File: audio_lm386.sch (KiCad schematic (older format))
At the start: 14 parts, among them J1 Screw_Terminal_01x02, J2 Screw_Terminal_01x02, J3 ST-025, U1 LM386

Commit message: добавлен предусилитель с пинами для подключения потенциометра
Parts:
- added C2: 47n, Capacitor_SMD:C_0805_2012Metric, symbol Device:C
- added C3, C4: 10uF, Capacitor_SMD:C_1206_3216Metric, symbol Device:CP
- added C5: 2n2, Capacitor_SMD:C_0805_2012Metric, symbol Device:C
- added J2: Screw_Terminal_01x03, Connector_PinHeader_2.54mm:PinHeader_1x03_P2.54mm_Vertical, symbol Connector:Screw_Terminal_01x03
- added Q1: MMBT5551L, Package_TO_SOT_SMD:SOT-23, symbol Transistor_BJT:MMBT5551L
- added R2, R3, R4, R5, R6: 10k, Resistor_SMD:R_0805_2012Metric, symbol Device:R
- J4: renamed from J3; footprint Connector_Audio:Jack_3.5mm_CUI_SJ1-3533NG_Horizontal_CircularHoles -> AM_Radio:ST-025 audio_jack
- renumbered C6 to C10, C3 to C6, C2 to C7, C4 to C8, C5 to C9, J2 to J3, R3 to R7, R2 to R8
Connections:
- net GND: now also C3.2, C5.2, J2.3 (Pin_3), R5.1
- net at C1.1, R1.1: now also C2.2; no longer U1.2 (-)
- net at C8.1, J3.1 (Pin_1), U1.6 (V+): now also R3.2
- new net: C5.1, R6.2, U1.2 (-)
- new net: C2.1, Q1.1 (B), R2.1
- new net: Q1.2 (E), R5.2
- new net: C4.1, Q1.3 (C), R2.2, R4.1
- new net: C3.1, R3.1, R4.2
- new net: C4.2, J2.1 (Pin_1)
- new net: J2.2 (Pin_2), R6.1
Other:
- moved on the sheet: C1, C10, C6, C7, C8, C9, FB1, J1, J3, J4, R1, R7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

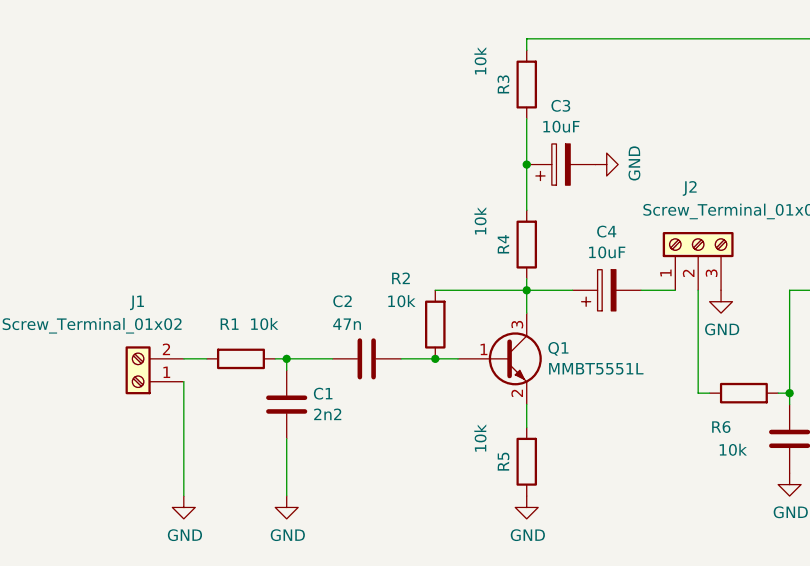
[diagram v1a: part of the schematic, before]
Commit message: выполнена трассировка для предусилителя с пинами для подключения потенциометра
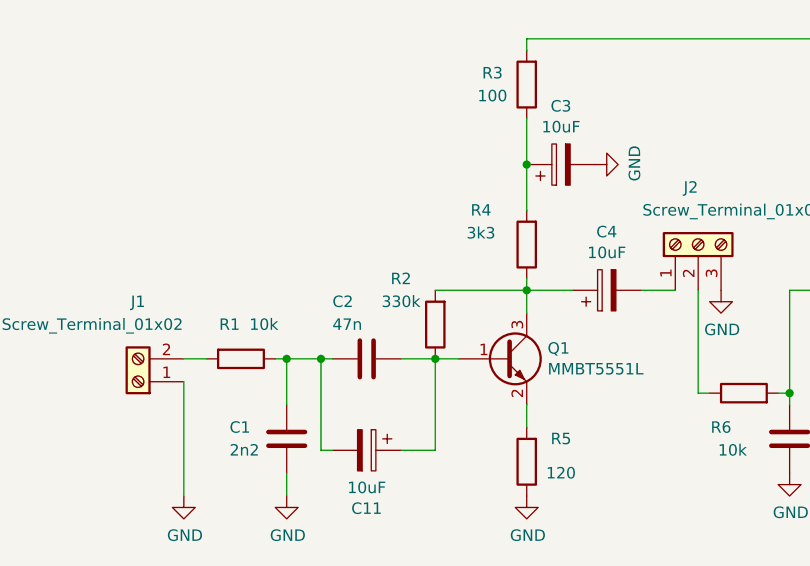
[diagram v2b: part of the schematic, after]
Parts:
- added C11: 10uF, Capacitor_SMD:C_1206_3216Metric, symbol Device:CP
- R2: value 10k -> 330k
- R3: value 10k -> 100
- R4: value 10k -> 3k3
- R5: value 10k -> 120
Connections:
- net at C1.1, C2.2, R1.1: now also C11.2
- net at C2.1, Q1.1 (B), R2.1: now also C11.1
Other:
- moved on the sheet: C1
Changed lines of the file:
@@
 L Device:C C1
 U 1 1 5DBE0A9F
-P 3600 3500
-F 0 "C1" H 3715 3546 50  0000 L CNN
-F 1 "2n2" H 3715 3455 50  0000 L CNN
-F 2 "Capacitor_SMD:C_0805_2012Metric" H 3638 3350 50  0001 C CNN
-F 3 "~" H 3600 3500 50  0001 C CNN
-F 4 "0805-2.2nF 50V" H 3600 3500 50  0001 C CNN "PartNumber"
-F 5 "GRM2165C1H222GA01D" H 3600 3500 50  0001 C CNN "ManufacturePartNumber"
-	1    3600 3500
+P 3600 3650
+F 0 "C1" H 3350 3700 50  0000 L CNN
+F 1 "2n2" H 3350 3600 50  0000 L CNN
+F 2 "Capacitor_SMD:C_0805_2012Metric" H 3638 3500 50  0001 C CNN
+F 3 "~" H 3600 3650 50  0001 C CNN
+F 4 "0805-2.2nF 50V" H 3600 3650 50  0001 C CNN "PartNumber"
+F 5 "GRM2165C1H222GA01D" H 3600 3650 50  0001 C CNN "ManufacturePartNumber"
+	1    3600 3650
 	1    0    0    -1
 $EndComp
@@
 Wire Wire Line
 	6350 3250 6350 3200
-Wire Wire Line
-	3600 3300 3600 3350
 $Comp
 L Device:R R1
@@
 U 1 1 5E2DB639
 P 4650 2800
-F 0 "R4" V 4750 2800 50  0000 C CNN
-F 1 "10k" V 4850 2700 50  0000 C CNN
+F 0 "R4" H 4850 2650 50  0000 C CNN
+F 1 "3k3" H 4850 2750 50  0000 C CNN
 F 2 "Resistor_SMD:R_0805_2012Metric" V 4580 2800 50  0001 C CNN
 F 3 "~" H 4650 2800 50  0001 C CNN
@@
 U 1 1 5E2DBC57
 P 4650 3750
-F 0 "R5" V 4750 3750 50  0000 C CNN
-F 1 "10k" V 4850 3650 50  0000 C CNN
+F 0 "R5" H 4500 3650 50  0000 C CNN
+F 1 "120" H 4500 3800 50  0000 C CNN
 F 2 "Resistor_SMD:R_0805_2012Metric" V 4580 3750 50  0001 C CNN
 F 3 "~" H 4650 3750 50  0001 C CNN
@@
 P 4250 3150
 F 0 "R2" H 4400 2950 50  0000 C CNN
-F 1 "10k" H 4400 3050 50  0000 C CNN
+F 1 "330k" H 4400 3050 50  0000 C CNN
 F 2 "Resistor_SMD:R_0805_2012Metric" V 4180 3150 50  0001 C CNN
 F 3 "~" H 4250 3150 50  0001 C CNN
@@
 $EndComp
 Wire Wire Line
-	3600 3300 3800 3300
+	3600 3300 3750 3300
 Connection ~ 3600 3300
 Wire Wire Line
@@
 U 1 1 5E32B944
 P 4650 2100
-F 0 "R3" V 4750 2100 50  0000 C CNN
-F 1 "10k" V 4850 2000 50  0000 C CNN
+F 0 "R3" H 4800 2050 50  0000 C CNN
+F 1 "100" H 4800 2150 50  0000 C CNN
 F 2 "Resistor_SMD:R_0805_2012Metric" V 4580 2100 50  0001 C CNN
 F 3 "~" H 4650 2100 50  0001 C CNN
@@
 Wire Wire Line
 	3150 3400 3150 3900
-Wire Wire Line
-	3600 3650 3600 3900
 $Comp
 L Device:CP C4
@@
 	1    0    0    -1
 $EndComp
+$Comp
+L Device:CP C11
+U 1 1 5E2E33AC
+P 3950 3700
+F 0 "C11" V 4205 3700 50  0000 C CNN
+F 1 "10uF" V 4114 3700 50  0000 C CNN
+F 2 "Capacitor_SMD:C_1206_3216Metric" H 3988 3550 50  0001 C CNN
+F 3 "~" H 3950 3700 50  0001 C CNN
+	1    3950 3700
+	0    1    1    0
+$EndComp
+Wire Wire Line
+	4100 3700 4250 3700
+Wire Wire Line
+	4250 3700 4250 3300
+Wire Wire Line
+	3800 3700 3750 3700
+Wire Wire Line
+	3750 3700 3750 3300
+Connection ~ 3750 3300
+Wire Wire Line
+	3750 3300 3800 3300
+Wire Wire Line
+	3600 3300 3600 3500
+Wire Wire Line
+	3600 3900 3600 3800
 $EndSCHEMATC
